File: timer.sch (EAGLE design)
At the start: 58 parts, among them IC1 CD4060, IC2 7805TV, K1 ZF112

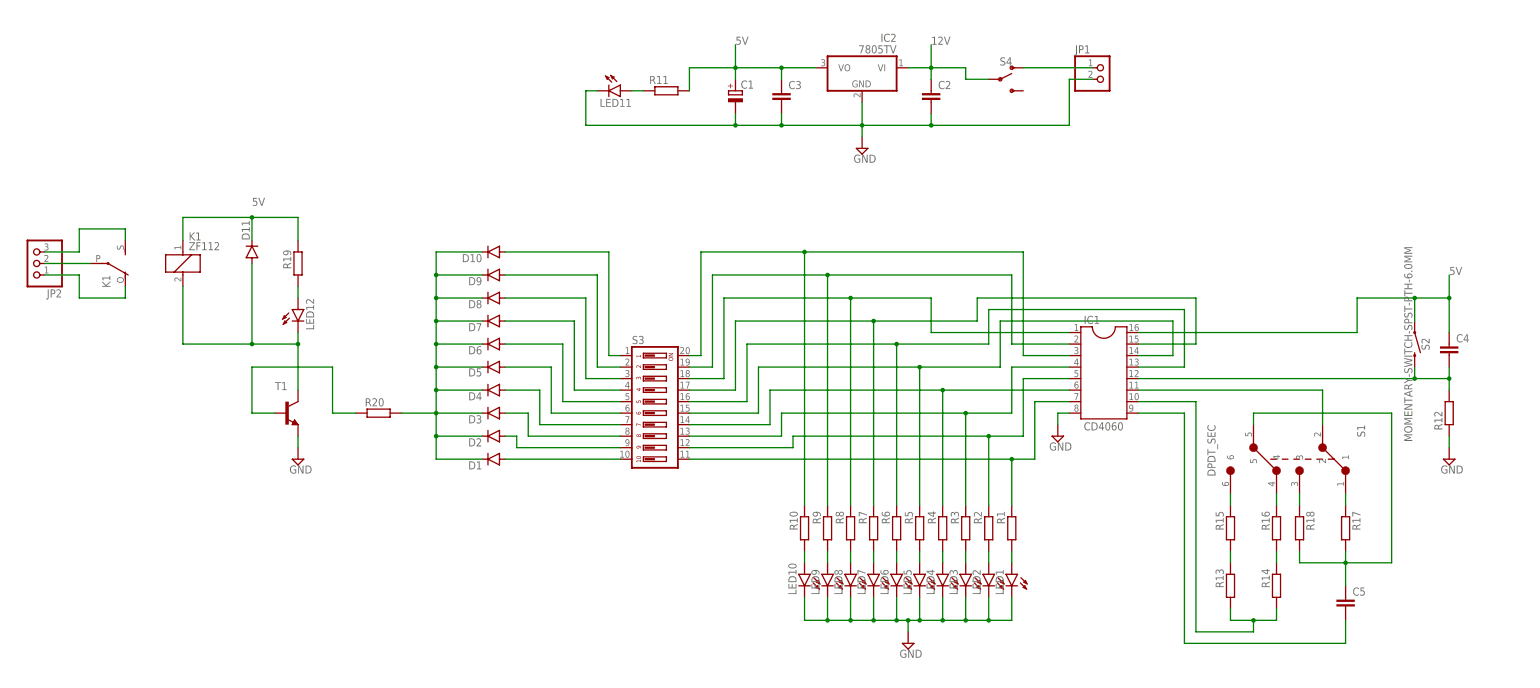
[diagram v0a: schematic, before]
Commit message: Values + OS Logo + Titlesheet
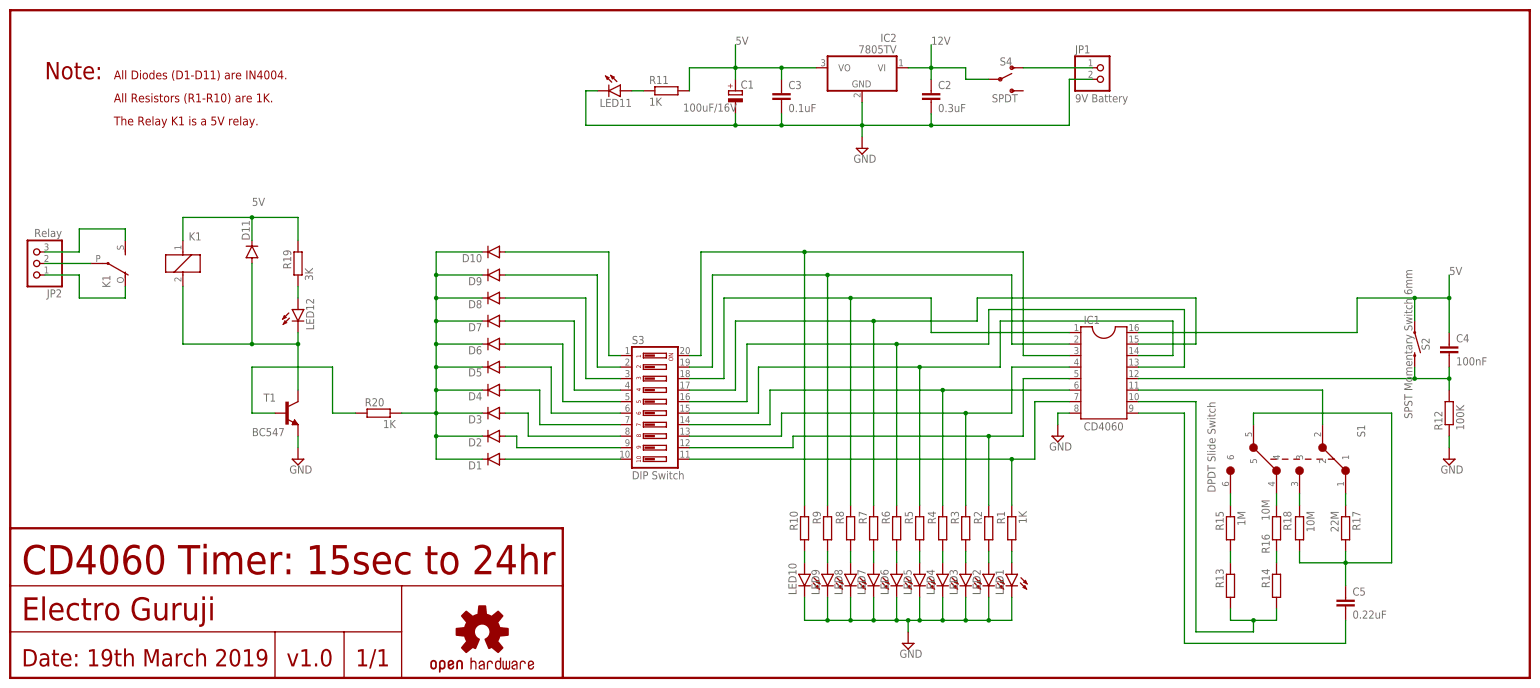
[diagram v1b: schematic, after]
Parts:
- added LOGO1: OSHW-LOGOS-COPPER, SparkFun-Aesthetics:OSHW-LOGOS-COPPER
- C1: value (none) -> 100uF/16V
- C2: value (none) -> 0.3uF
- C3: value (none) -> 0.1uF
- C4: value (none) -> 100nF
- C5: value (none) -> 0.22uF
- JP1: value (none) -> 9V Battery
- JP2: value (none) -> Relay
- K1: value ZF112 -> 5V
- R1, R11, R20: value (none) -> 1K
- R12: value (none) -> 100K
- R15: value (none) -> 1M
- R16, R18: value (none) -> 10M
- R17: value (none) -> 22M
- R19: value (none) -> 3K
- S1: value DPDT_SEC -> DPDT Slide Switch
- S2: value MOMENTARY-SWITCH-SPST-PTH-6.0MM -> SPST Momentary Switch 6mm
- S3: value (none) -> DIP Switch
- S4: value (none) -> SPDT
- T1: value (none) -> BC547
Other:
- note added: "1/1"
- note added: "All Diodes (D1-D11) are IN4004."
- note added: "All Resistors (R1-R10) are 1K."
- note added: "CD4060 Timer: 15sec to 24hr"
- note added: "Date: 19th March 2019"
- note added: "Electro Guruji"
- note added: "Note:"
- note added: "The Relay K1 is a 5V relay."
- note added: "v1.0"

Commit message: Changed Relay Output Connector
Pinhead JP2 changed to screw terminal J1
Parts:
- removed JP2: Relay, pinhead:PINHD-1X3
- added J1: Relay, SparkFun-Connectors:CONN_03-SCREW-5MM
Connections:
- net N$48: now also J1.2; no longer JP2.2
- net N$49: now also J1.3; no longer JP2.3
- net N$50: now also J1.1; no longer JP2.1
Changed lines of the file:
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@@
 <layer number="230" name="230bmp" color="7" fill="1" visible="no" active="yes"/>
 <layer number="231" name="231bmp" color="7" fill="1" visible="no" active="yes"/>
+<layer number="232" name="Eagle3D_PG2" color="7" fill="1" visible="yes" active="yes"/>
+<layer number="233" name="Eagle3D_PG3" color="7" fill="1" visible="yes" active="yes"/>
 <layer number="248" name="Housing" color="7" fill="1" visible="no" active="yes"/>
 <layer number="249" name="Edge" color="7" fill="1" visible="no" active="yes"/>
@@
 <part name="R20" library="resistor" library_urn="urn:adsk.eagle:library:348" deviceset="R-EU_" device="0207/10" package3d_urn="urn:adsk.eagle:package:23491/2" value="1K"/>
 <part name="SUPPLY5" library="supply2" library_urn="urn:adsk.eagle:library:372" deviceset="GND" device=""/>
-<part name="JP2" library="pinhead" library_urn="urn:adsk.eagle:library:325" deviceset="PINHD-1X3" device="" package3d_urn="urn:adsk.eagle:package:22458/2" value="Relay"/>
 <part name="S4" library="SparkFun-Switches" library_urn="urn:adsk.eagle:library:535" deviceset="SWITCH-SPDT" device="-PTH-11.6X4.0MM" value="SPDT"/>
 <part name="LOGO1" library="SparkFun-Aesthetics" library_urn="urn:adsk.eagle:library:507" deviceset="OSHW-LOGO" device="S-COPPER"/>
+<part name="J1" library="SparkFun-Connectors" library_urn="urn:adsk.eagle:library:513" deviceset="CONN_03" device="-SCREW-5MM" value="Relay"/>
 </parts>
 <sheets>
@@
 <attribute name="VALUE" x="-146.685" y="-23.495" size="1.778" layer="96"/>
 </instance>
-<instance part="JP2" gate="A" x="-203.2" y="22.86" smashed="yes" rot="R180">
-<attribute name="NAME" x="-196.85" y="17.145" size="1.778" layer="95" rot="R180"/>
-<attribute name="VALUE" x="-196.85" y="30.48" size="1.778" layer="96" rot="R180"/>
-</instance>
 <instance part="S4" gate="1" x="10.16" y="63.5" smashed="yes">
 <attribute name="NAME" x="11.43" y="66.548" size="1.778" layer="95" font="vector" align="bottom-center"/>
@@
 </instance>
 <instance part="LOGO1" gate="G$1" x="-104.14" y="-58.42" smashed="yes"/>
+<instance part="J1" gate="J$1" x="-203.2" y="22.86" smashed="yes">
+<attribute name="VALUE" x="-205.74" y="15.494" size="1.778" layer="96" font="vector"/>
+<attribute name="NAME" x="-205.74" y="28.448" size="1.778" layer="95" font="vector"/>
+</instance>
 </instances>
 <busses>
@@
 <segment>
 <pinref part="K1" gate="2" pin="P"/>
-<pinref part="JP2" gate="A" pin="2"/>
-<wire x1="-190.5" y1="22.86" x2="-200.66" y2="22.86" width="0.1524" layer="91"/>
+<wire x1="-190.5" y1="22.86" x2="-195.58" y2="22.86" width="0.1524" layer="91"/>
+<pinref part="J1" gate="J$1" pin="2"/>
 </segment>
 </net>
 <net name="N$49" class="0">
 <segment>
-<pinref part="JP2" gate="A" pin="3"/>
-<wire x1="-200.66" y1="25.4" x2="-193.04" y2="25.4" width="0.1524" layer="91"/>
+<wire x1="-195.58" y1="25.4" x2="-193.04" y2="25.4" width="0.1524" layer="91"/>
 <wire x1="-193.04" y1="25.4" x2="-193.04" y2="30.48" width="0.1524" layer="91"/>
 <wire x1="-193.04" y1="30.48" x2="-182.88" y2="30.48" width="0.1524" layer="91"/>
 <pinref part="K1" gate="2" pin="S"/>
 <wire x1="-182.88" y1="30.48" x2="-182.88" y2="27.94" width="0.1524" layer="91"/>
+<pinref part="J1" gate="J$1" pin="3"/>
 </segment>
 </net>
@@
 <wire x1="-182.88" y1="15.24" x2="-193.04" y2="15.24" width="0.1524" layer="91"/>
 <wire x1="-193.04" y1="15.24" x2="-193.04" y2="20.32" width="0.1524" layer="91"/>
-<pinref part="JP2" gate="A" pin="1"/>
-<wire x1="-193.04" y1="20.32" x2="-200.66" y2="20.32" width="0.1524" layer="91"/>
-</segment>
-</net>
+<wire x1="-193.04" y1="20.32" x2="-195.58" y2="20.32" width="0.1524" layer="91"/>
+<pinref part="J1" gate="J$1" pin="1"/>
+</segment>
+</net>

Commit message: Added values of R13,R14
910K Ohm
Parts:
- R13, R14: value (none) -> 910K
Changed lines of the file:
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@@
 <part name="R11" library="resistor" library_urn="urn:adsk.eagle:library:348" deviceset="R-EU_" device="0207/10" package3d_urn="urn:adsk.eagle:package:23491/2" value="1K"/>
 <part name="R12" library="resistor" library_urn="urn:adsk.eagle:library:348" deviceset="R-EU_" device="0207/10" package3d_urn="urn:adsk.eagle:package:23491/2" value="100K"/>
-<part name="R13" library="resistor" library_urn="urn:adsk.eagle:library:348" deviceset="R-EU_" device="0207/10" package3d_urn="urn:adsk.eagle:package:23491/2"/>
-<part name="R14" library="resistor" library_urn="urn:adsk.eagle:library:348" deviceset="R-EU_" device="0207/10" package3d_urn="urn:adsk.eagle:package:23491/2"/>
+<part name="R13" library="resistor" library_urn="urn:adsk.eagle:library:348" deviceset="R-EU_" device="0207/10" package3d_urn="urn:adsk.eagle:package:23491/2" value="910K"/>
+<part name="R14" library="resistor" library_urn="urn:adsk.eagle:library:348" deviceset="R-EU_" device="0207/10" package3d_urn="urn:adsk.eagle:package:23491/2" value="910K"/>
 <part name="R15" library="resistor" library_urn="urn:adsk.eagle:library:348" deviceset="R-EU_" device="0207/10" package3d_urn="urn:adsk.eagle:package:23491/2" value="1M"/>
 <part name="R16" library="resistor" library_urn="urn:adsk.eagle:library:348" deviceset="R-EU_" device="0207/10" package3d_urn="urn:adsk.eagle:package:23491/2" value="10M"/>
